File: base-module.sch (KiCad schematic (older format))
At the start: 0 parts

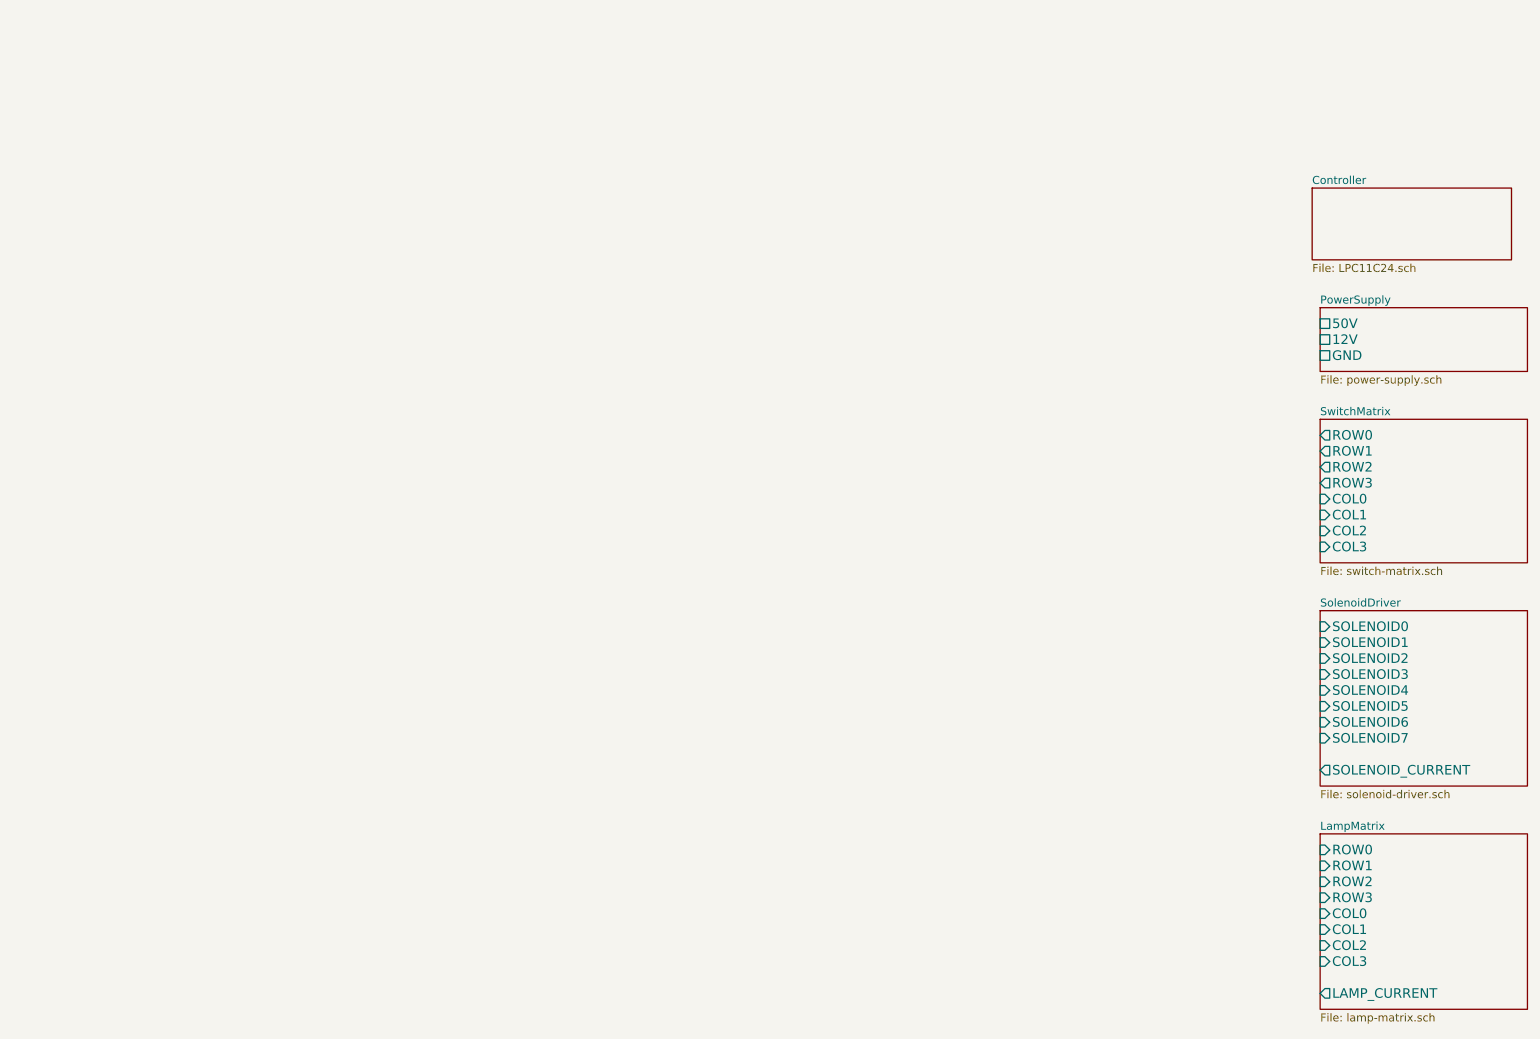
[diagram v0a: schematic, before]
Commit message: Changed the controller symbol for the LPC11C24 added some of the support components,played with the larger blocks
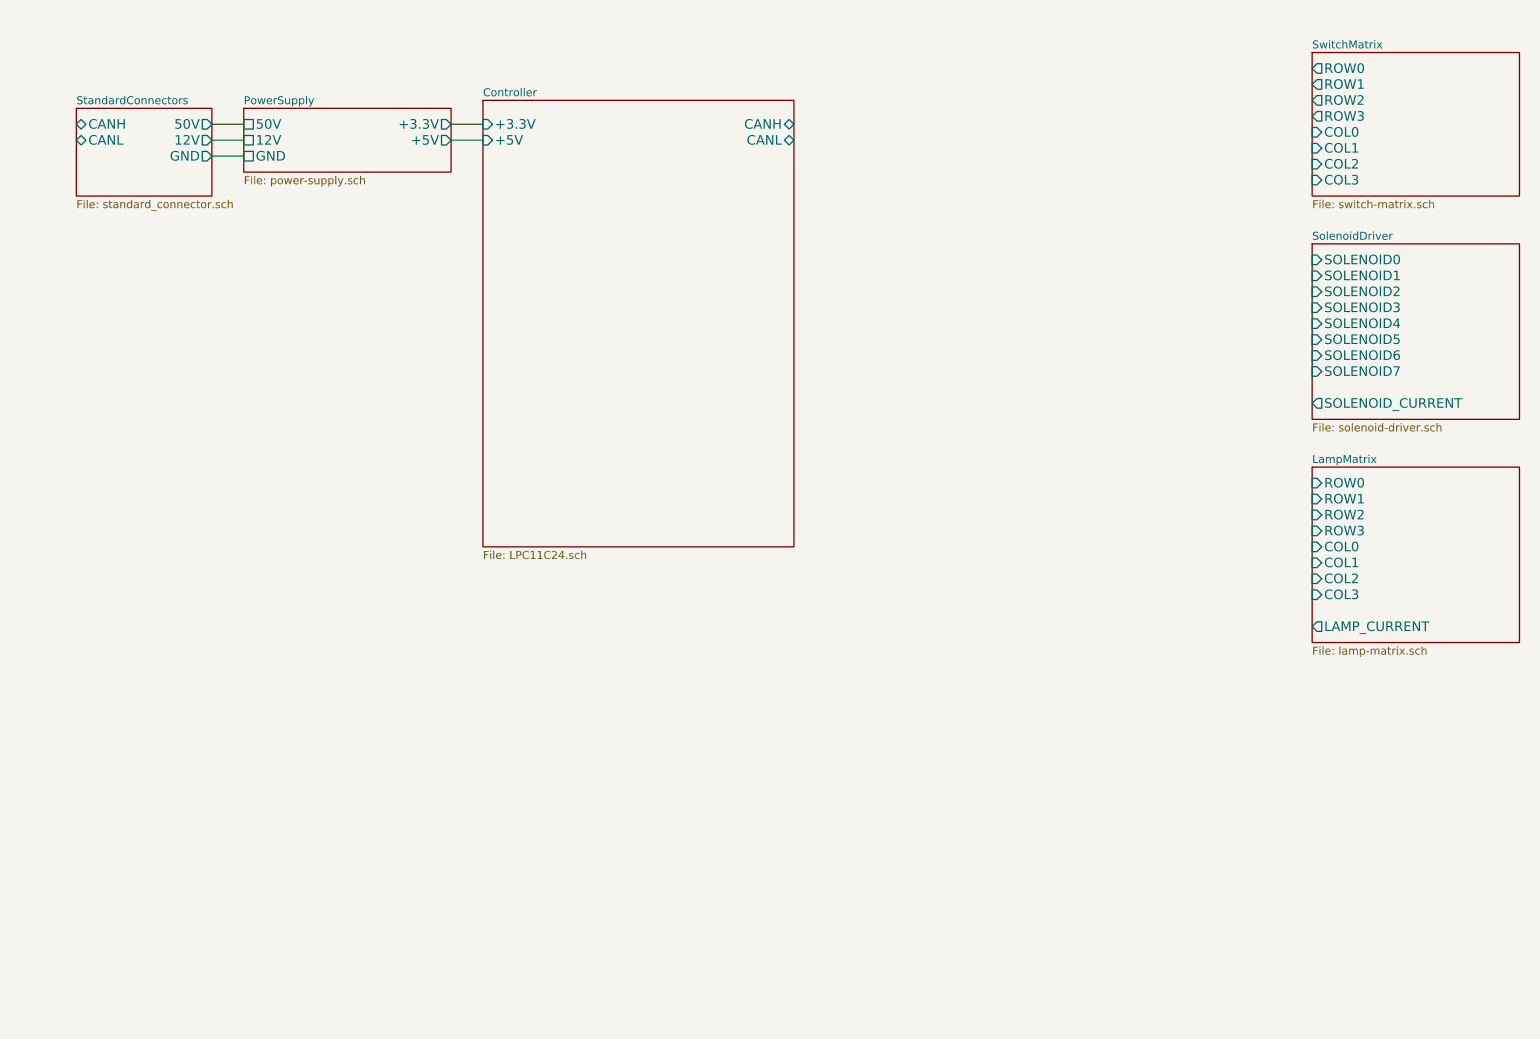
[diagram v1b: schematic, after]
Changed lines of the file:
@@
-EESchema Schematic File Version 2  date 4/14/2013 3:01:00 AM
+EESchema Schematic File Version 2  date 4/14/2013 3:47:51 AM
 LIBS:power
 LIBS:device
@@
 $EndDescr
 $Sheet
-S 8800 3400 1300 900
+S 8750 1100 1300 900
 U 51638E9B
 F0 "SwitchMatrix" 50
 F1 "switch-matrix.sch" 50
-F2 "ROW0" O L 8800 3500 60
-F3 "ROW1" O L 8800 3600 60
-F4 "ROW2" O L 8800 3700 60
-F5 "ROW3" O L 8800 3800 60
-F6 "COL0" I L 8800 3900 60
-F7 "COL1" I L 8800 4000 60
-F8 "COL2" I L 8800 4100 60
-F9 "COL3" I L 8800 4200 60
+F2 "ROW0" O L 8750 1200 60
+F3 "ROW1" O L 8750 1300 60
+F4 "ROW2" O L 8750 1400 60
+F5 "ROW3" O L 8750 1500 60
+F6 "COL0" I L 8750 1600 60
+F7 "COL1" I L 8750 1700 60
+F8 "COL2" I L 8750 1800 60
+F9 "COL3" I L 8750 1900 60
 $EndSheet
 $Sheet
-S 8800 6000 1300 1100
+S 8750 3700 1300 1100
 U 51638EC2
 F0 "LampMatrix" 50
 F1 "lamp-matrix.sch" 50
-F2 "ROW0" I L 8800 6100 60
-F3 "ROW1" I L 8800 6200 60
-F4 "ROW2" I L 8800 6300 60
-F5 "ROW3" I L 8800 6400 60
-F6 "COL0" I L 8800 6500 60
-F7 "COL1" I L 8800 6600 60
-F8 "COL2" I L 8800 6700 60
-F9 "COL3" I L 8800 6800 60
-F10 "LAMP_CURRENT" O L 8800 7000 60
+F2 "ROW0" I L 8750 3800 60
+F3 "ROW1" I L 8750 3900 60
+F4 "ROW2" I L 8750 4000 60
+F5 "ROW3" I L 8750 4100 60
+F6 "COL0" I L 8750 4200 60
+F7 "COL1" I L 8750 4300 60
+F8 "COL2" I L 8750 4400 60
+F9 "COL3" I L 8750 4500 60
+F10 "LAMP_CURRENT" O L 8750 4700 60
 $EndSheet
 $Sheet
-S 8800 2700 1300 400
+S 8750 2300 1300 1100
+U 51638EDE
+F0 "SolenoidDriver" 50
+F1 "solenoid-driver.sch" 50
+F2 "SOLENOID0" I L 8750 2400 60
+F3 "SOLENOID1" I L 8750 2500 60
+F4 "SOLENOID2" I L 8750 2600 60
+F5 "SOLENOID3" I L 8750 2700 60
+F6 "SOLENOID4" I L 8750 2800 60
+F7 "SOLENOID5" I L 8750 2900 60
+F8 "SOLENOID6" I L 8750 3000 60
+F9 "SOLENOID7" I L 8750 3100 60
+F10 "SOLENOID_CURRENT" O L 8750 3300 60
+$EndSheet
+$Sheet
+S 3550 1400 1950 2800
+U 516A58DE
+F0 "Controller" 50
+F1 "LPC11C24.sch" 50
+F2 "CANH" B R 5500 1550 60
+F3 "CANL" B R 5500 1650 60
+F4 "+3.3V" I L 3550 1550 60
+F5 "+5V" I L 3550 1650 60
+$EndSheet
+$Sheet
+S 2050 1450 1300 400
 U 51638FEE
 F0 "PowerSupply" 50
 F1 "power-supply.sch" 50
-F2 "50V" U L 8800 2800 60
-F3 "12V" U L 8800 2900 60
-F4 "GND" U L 8800 3000 60
+F2 "50V" U L 2050 1550 60
+F3 "12V" U L 2050 1650 60
+F4 "GND" U L 2050 1750 60
+F5 "+3.3V" O R 3350 1550 60
+F6 "+5V" O R 3350 1650 60
 $EndSheet
+Wire Wire Line
+	3350 1550 3550 1550
+Wire Wire Line
+	3550 1650 3350 1650
 $Sheet
-S 8800 4600 1300 1100
-U 51638EDE
-F0 "SolenoidDriver" 50
-F1 "solenoid-driver.sch" 50
-F2 "SOLENOID0" I L 8800 4700 60
-F3 "SOLENOID1" I L 8800 4800 60
-F4 "SOLENOID2" I L 8800 4900 60
-F5 "SOLENOID3" I L 8800 5000 60
-F6 "SOLENOID4" I L 8800 5100 60
-F7 "SOLENOID5" I L 8800 5200 60
-F8 "SOLENOID6" I L 8800 5300 60
-F9 "SOLENOID7" I L 8800 5400 60
-F10 "SOLENOID_CURRENT" O L 8800 5600 60
+S 1000 1450 850  550
+U 516AEB88
+F0 "StandardConnectors" 50
+F1 "standard_connector.sch" 50
+F2 "CANH" B L 1000 1550 60
+F3 "CANL" B L 1000 1650 60
+F4 "50V" O R 1850 1550 60
+F5 "12V" O R 1850 1650 60
+F6 "GND" O R 1850 1750 60
 $EndSheet
-$Sheet
-S 8750 1950 1250 450
-U 516A58DE
-F0 "Controller" 50
-F1 "LPC11C24.sch" 50
-$EndSheet
+Wire Wire Line
+	1850 1750 2050 1750
+Wire Wire Line
+	1850 1650 2050 1650
+Wire Wire Line
+	1850 1550 2050 1550
 $EndSCHEMATC

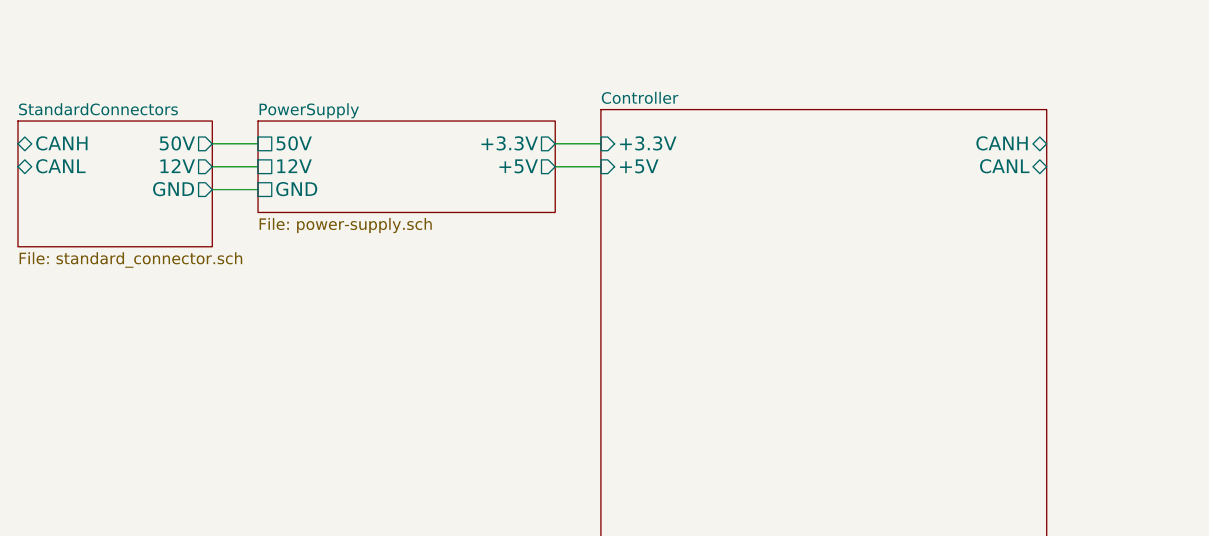
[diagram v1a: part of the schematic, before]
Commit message: changed the voltage lbaels to global labels
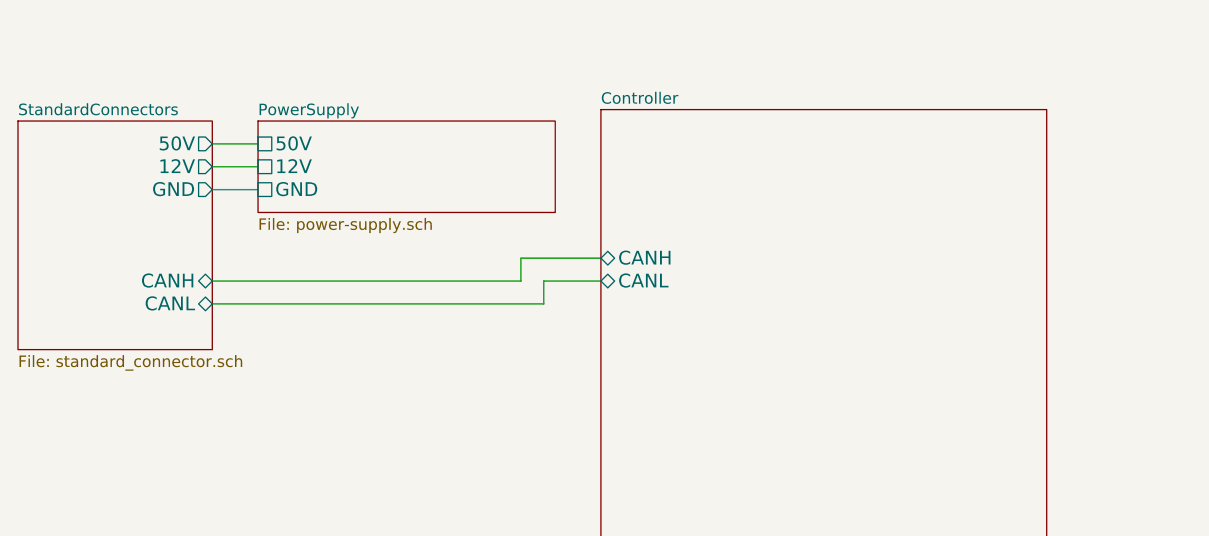
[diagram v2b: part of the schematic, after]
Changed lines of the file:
@@
-EESchema Schematic File Version 2  date 4/14/2013 3:47:51 AM
+EESchema Schematic File Version 2  date 4/14/2013 1:14:12 PM
 LIBS:power
 LIBS:device
@@
 $Descr USLetter 11000 8500
 encoding utf-8
-Sheet 1 6
+Sheet 1 7
 Title ""
 Date "14 apr 2013"
@@
 F0 "Controller" 50
 F1 "LPC11C24.sch" 50
-F2 "CANH" B R 5500 1550 60
-F3 "CANL" B R 5500 1650 60
-F4 "+3.3V" I L 3550 1550 60
-F5 "+5V" I L 3550 1650 60
+F2 "CANH" B L 3550 2050 60
+F3 "CANL" B L 3550 2150 60
 $EndSheet
 $Sheet
-S 2050 1450 1300 400
-U 51638FEE
-F0 "PowerSupply" 50
-F1 "power-supply.sch" 50
-F2 "50V" U L 2050 1550 60
-F3 "12V" U L 2050 1650 60
-F4 "GND" U L 2050 1750 60
-F5 "+3.3V" O R 3350 1550 60
-F6 "+5V" O R 3350 1650 60
-$EndSheet
-Wire Wire Line
-	3350 1550 3550 1550
-Wire Wire Line
-	3550 1650 3350 1650
-$Sheet
-S 1000 1450 850  550
+S 1000 1450 850  1000
 U 516AEB88
 F0 "StandardConnectors" 50
 F1 "standard_connector.sch" 50
-F2 "CANH" B L 1000 1550 60
-F3 "CANL" B L 1000 1650 60
+F2 "CANH" B R 1850 2150 60
+F3 "CANL" B R 1850 2250 60
 F4 "50V" O R 1850 1550 60
 F5 "12V" O R 1850 1650 60
@@
 Wire Wire Line
 	1850 1550 2050 1550
+$Sheet
+S 2050 1450 1300 400
+U 51638FEE
+F0 "PowerSupply" 50
+F1 "power-supply.sch" 50
+F2 "50V" U L 2050 1550 60
+F3 "12V" U L 2050 1650 60
+F4 "GND" U L 2050 1750 60
+$EndSheet
+Wire Wire Line
+	3200 2150 1850 2150
+Wire Wire Line
+	3200 2050 3200 2150
+Wire Wire Line
+	3200 2050 3550 2050
+Wire Wire Line
+	3550 2150 3300 2150
+Wire Wire Line
+	3300 2150 3300 2250
+Wire Wire Line
+	3300 2250 1850 2250
 $EndSCHEMATC

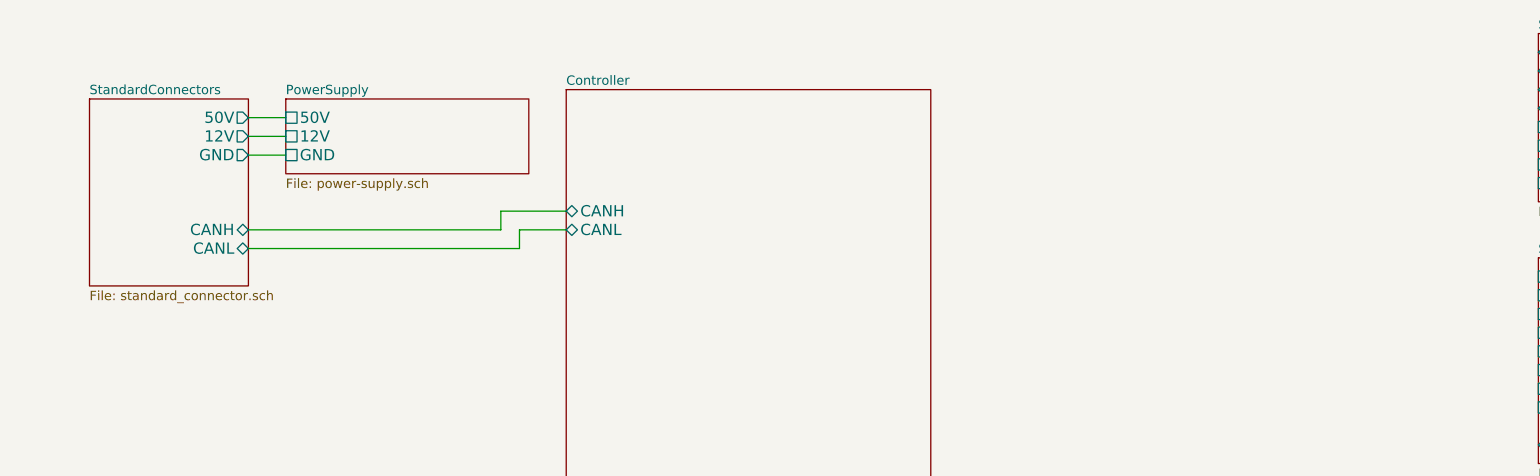
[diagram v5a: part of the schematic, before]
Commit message: power updated still need to add underpad also changed input connector to 5 pin and added fuses, added current sense with op-amp for solinoids
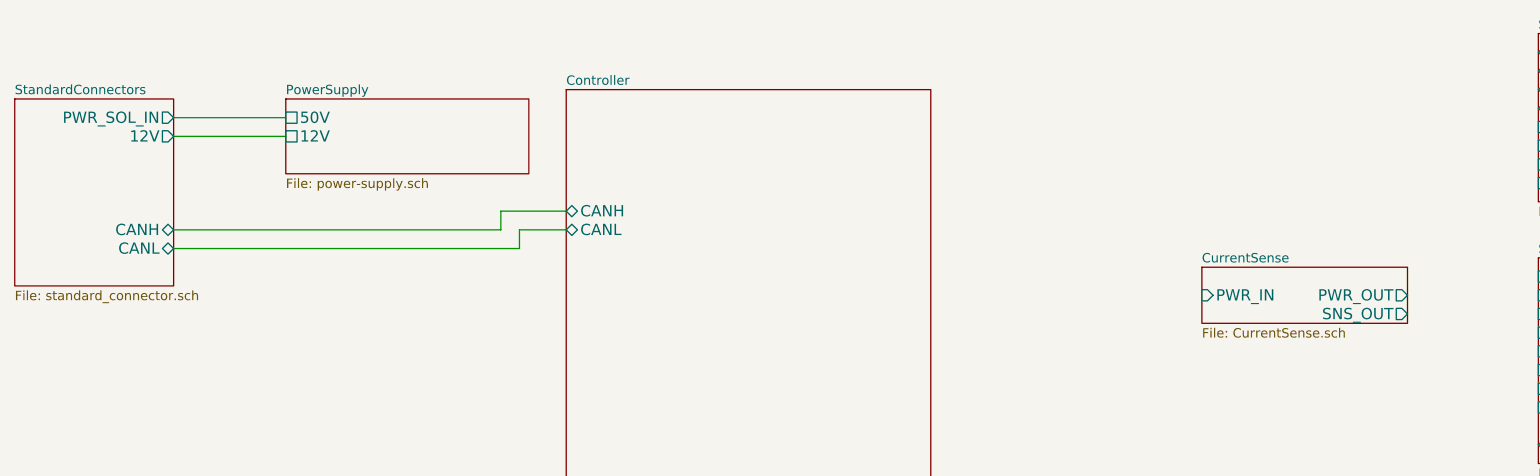
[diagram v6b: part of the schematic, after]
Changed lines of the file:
@@
-EESchema Schematic File Version 2  date 4/15/2013 1:22:57 AM
+EESchema Schematic File Version 2  date 4/16/2013 12:48:50 AM
 LIBS:power
 LIBS:device
@@
 LIBS:pinball_components
 LIBS:micro-controller
+LIBS:CurrentSense
+LIBS:pinball-power
 LIBS:base-module-cache
 EELAYER 27 0
@@
 $Descr USLetter 11000 8500
 encoding utf-8
-Sheet 1 7
+Sheet 1 8
 Title ""
-Date "15 apr 2013"
+Date "16 apr 2013"
 Rev ""
 Comp ""
@@
 F3 "CANL" B L 3550 2150 60
 $EndSheet
-$Sheet
-S 1000 1450 850  1000
-U 516AEB88
-F0 "StandardConnectors" 50
-F1 "standard_connector.sch" 50
-F2 "CANH" B R 1850 2150 60
-F3 "CANL" B R 1850 2250 60
-F4 "50V" O R 1850 1550 60
-F5 "12V" O R 1850 1650 60
-F6 "GND" O R 1850 1750 60
-$EndSheet
 Wire Wire Line
-	1850 1750 2050 1750
+	1450 1650 2050 1650
 Wire Wire Line
-	1850 1650 2050 1650
-Wire Wire Line
-	1850 1550 2050 1550
+	1450 1550 2050 1550
 $Sheet
 S 2050 1450 1300 400
@@
 F2 "50V" U L 2050 1550 60
 F3 "12V" U L 2050 1650 60
-F4 "GND" U L 2050 1750 60
 $EndSheet
 Wire Wire Line
-	3200 2150 1850 2150
+	3200 2150 1450 2150
 Wire Wire Line
 	3200 2050 3200 2150
@@
 	3300 2150 3300 2250
 Wire Wire Line
-	3300 2250 1850 2250
+	3300 2250 1450 2250
+$Sheet
+S 6950 2350 1100 300
+U 516CAB4E
+F0 "CurrentSense" 50
+F1 "CurrentSense.sch" 50
+F2 "PWR_IN" I L 6950 2500 60
+F3 "PWR_OUT" O R 8050 2500 60
+F4 "SNS_OUT" O R 8050 2600 60
+$EndSheet
+$Sheet
+S 600  1450 850  1000
+U 516AEB88
+F0 "StandardConnectors" 50
+F1 "standard_connector.sch" 50
+F2 "PWR_SOL_IN" O R 1450 1550 60
+F3 "CANH" B R 1450 2150 60
+F4 "CANL" B R 1450 2250 60
+F5 "12V" O R 1450 1650 60
+$EndSheet
 $EndSCHEMATC
